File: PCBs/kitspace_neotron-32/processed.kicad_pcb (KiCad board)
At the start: 4 copper layers, 166.9 x 140.7 mm, 97 parts, among them J1001 Conn_02x05, J101 Conn_02x06, J102 Conn_02x06, J103 Conn_02x04, J201 DIN-5 180 degree, J202 DIN-5 180 degree, J301 3.5mm Audio Jack TRS, J302 Conn_01x03_Male, J401 USB_B, J501 micro SD Card, J601 Conn_02x13_Header, J701 AVR-ISP-6, J702 DE9 Male, J703 DE9 Male, J704 Double-mini-DIN-6, J901 DB15HD_Female, SW401 SW_Push_DPDT_ON_OFF, SW402 SW_Push_DPDT_ON_MO, U1001 ICL3232CPZMAX, U101 EK-TM4C123GXL, U201 74LS14, U202 6N138, U401 TC1262-33, U601 MCP23S17_SP, U701 ATmega328-PU, U801 MCP7940N-xP, Y801 32,768 Hz

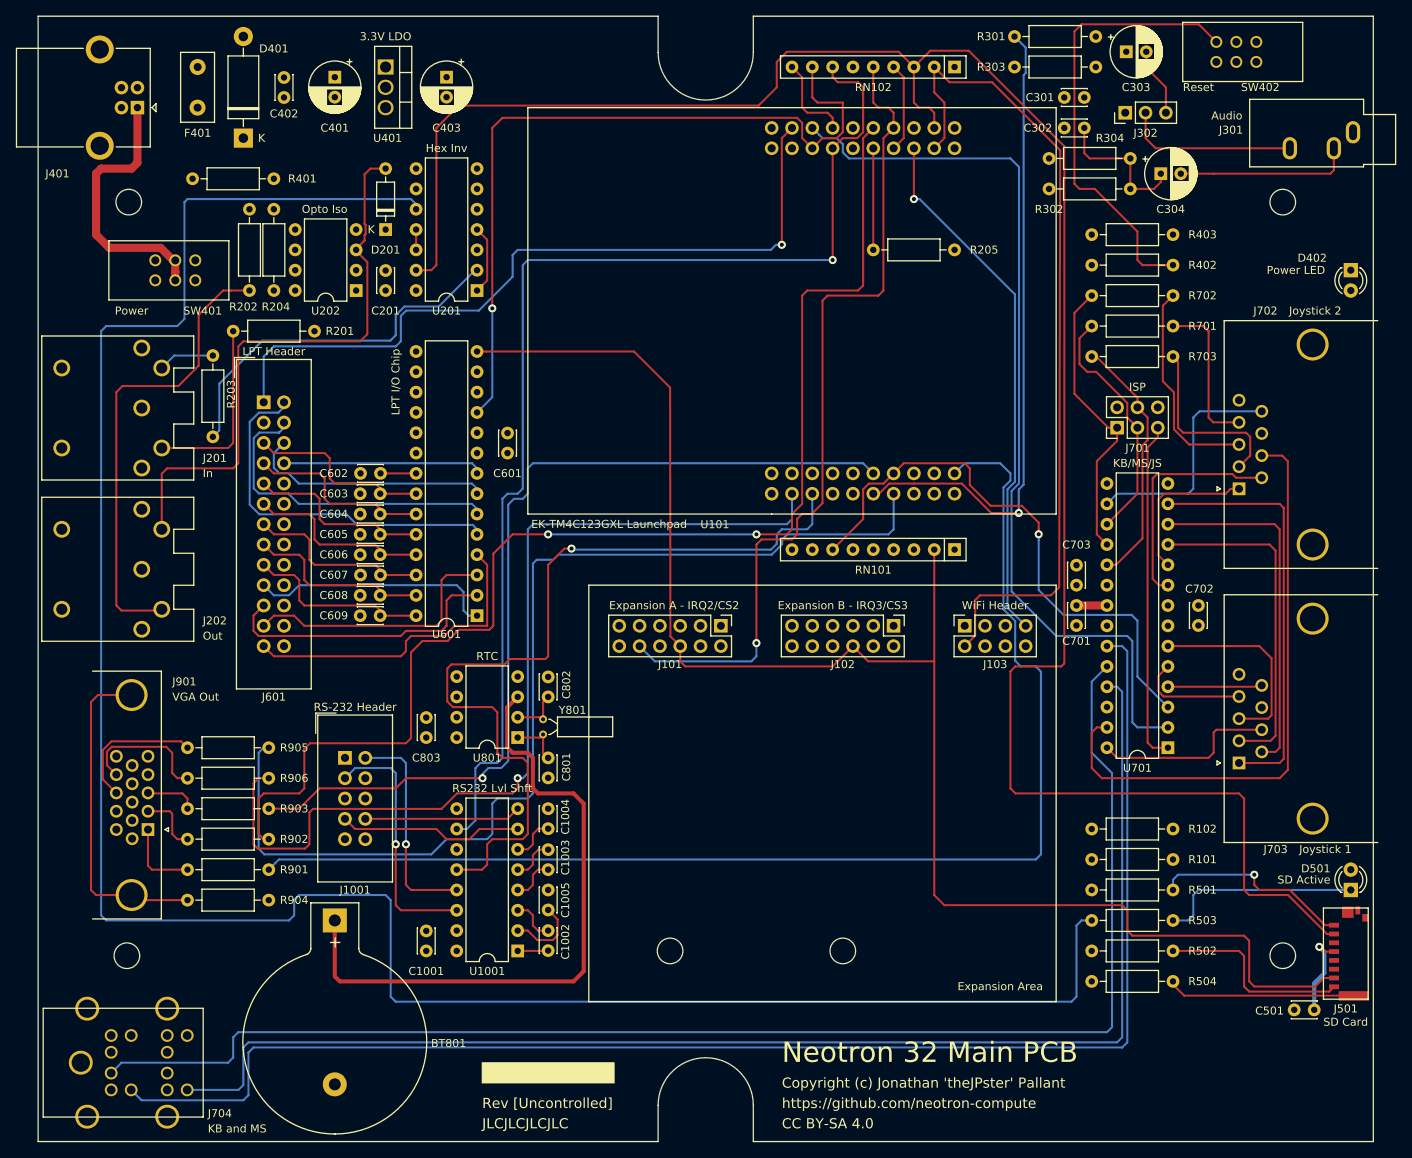
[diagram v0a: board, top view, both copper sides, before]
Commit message: recheck all circuits and clean up fill zone by rerouting the nets using freerouting and manually
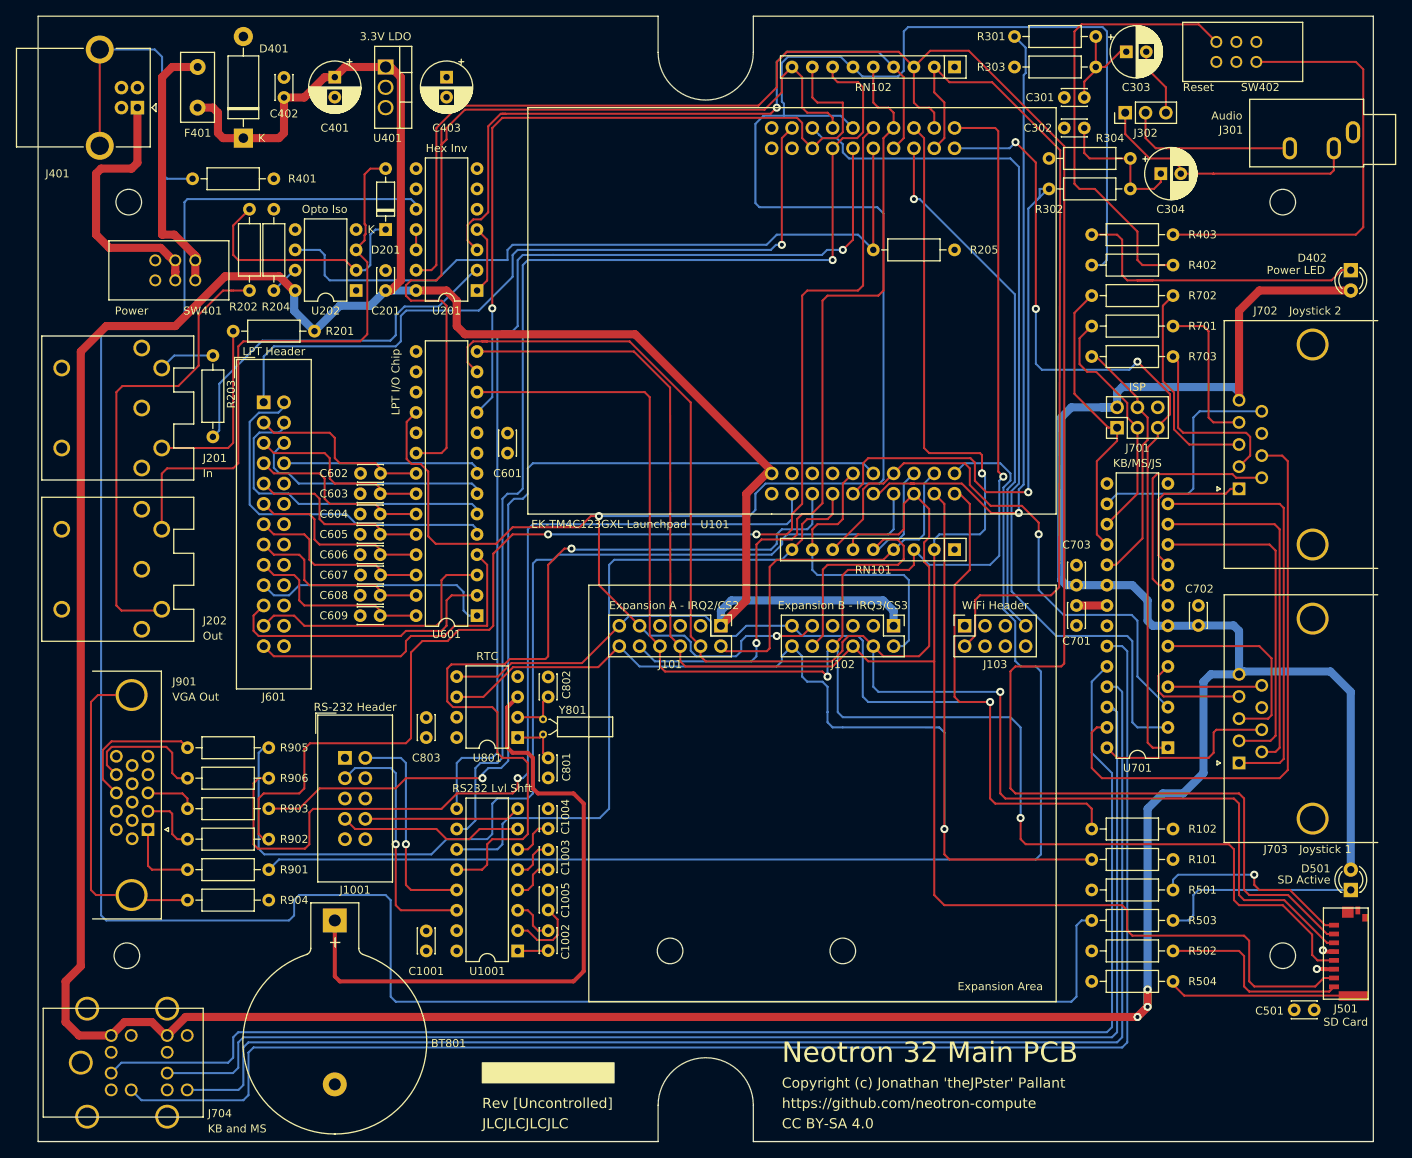
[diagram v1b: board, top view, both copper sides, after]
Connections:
- BT801 pad 2: (no net) -> GND
- C1001 pad 1: (no net) -> GND
- C1001 pad 2: (no net) -> +3V3
- C1004 pad 1: (no net) -> GND
- C1005 pad 1: (no net) -> +3V3
- C201 pad 1: (no net) -> +5V
- C201 pad 2: (no net) -> GND
- C301 pad 1: (no net) -> GND
- C301 pad 2: (no net) -> Net-(C301-Pad2)
- C302 pad 1: (no net) -> GND
- C303 pad 1: (no net) -> Net-(C301-Pad2)
- C401 pad 1: (no net) -> +5V
- C401 pad 2: (no net) -> GND
- C402 pad 1: (no net) -> +5V
- C402 pad 2: (no net) -> GND
- C403 pad 1: (no net) -> +3V3
- C403 pad 2: (no net) -> GND
- C501 pad 2: (no net) -> GND
- C601 pad 1: (no net) -> +3V3
- C601 pad 2: (no net) -> GND
- C602 pad 1: (no net) -> GND
- C603 pad 1: (no net) -> GND
- C604 pad 1: (no net) -> GND
- C605 pad 1: (no net) -> GND
- C606 pad 1: (no net) -> GND
- C607 pad 1: (no net) -> GND
- C608 pad 1: (no net) -> GND
- C609 pad 1: (no net) -> GND
- C701 pad 1: (no net) -> GND
- C702 pad 1: (no net) -> +5V
- C702 pad 2: (no net) -> GND
- C703 pad 1: (no net) -> +5V
- C703 pad 2: (no net) -> GND
- C801 pad 1: (no net) -> GND
- C802 pad 2: (no net) -> GND
- C803 pad 1: (no net) -> +3V3
- C803 pad 2: (no net) -> GND
- D201 pad 1: (no net) -> Net-(D201-Pad1)
- D401 pad 1: (no net) -> +5V
- D401 pad 2: (no net) -> GND
- D402 pad 1: (no net) -> Net-(D402-Pad1)
- D402 pad 2: (no net) -> +5V
- D501 pad 2: (no net) -> +5V
- F401 pad 1: (no net) -> +5V
- F401 pad 2: (no net) -> /Power/UNFUSED_5V
- J1001 pad 1: (no net) -> Net-(J1001-Pad1)
- J1001 pad 10: (no net) -> Net-(J1001-Pad10)
- J1001 pad 4: (no net) -> Net-(J1001-Pad4)
- J1001 pad 5: (no net) -> GND
- J1001 pad 6: (no net) -> Net-(J1001-Pad6)
- J1001 pad 9: (no net) -> Net-(J1001-Pad9)
- J101 pad 1: (no net) -> +5V
- J101 pad 11: (no net) -> /PA7_I2C_SDA
- J101 pad 12: (no net) -> /PA6_I2C_SCL
- J101 pad 2: (no net) -> /~PE3_IRQ2
- J101 pad 3: (no net) -> +3V3
- J101 pad 4: (no net) -> /PA5_SPI_MOSI
- J101 pad 5: (no net) -> GND
- J101 pad 7: (no net) -> GND
- J101 pad 8: (no net) -> /PA2_SPI_CLK
- J101 pad 9: (no net) -> /~RESET
- J102 pad 1: (no net) -> +5V
- J102 pad 10: (no net) -> /~PE2_SPI_CS3
- J102 pad 11: (no net) -> /PA7_I2C_SDA
- J102 pad 12: (no net) -> /PA6_I2C_SCL
- J102 pad 2: (no net) -> /~PD2_IRQ3
- J102 pad 3: (no net) -> +3V3
- J102 pad 4: (no net) -> /PA5_SPI_MOSI
- J102 pad 5: (no net) -> GND
- J102 pad 7: (no net) -> GND
- J102 pad 8: (no net) -> /PA2_SPI_CLK
- J102 pad 9: (no net) -> /~RESET
- J103 pad 1: (no net) -> +3V3
- J103 pad 3: (no net) -> Net-(J103-Pad3)
- J103 pad 4: (no net) -> Net-(J103-Pad4)
- J103 pad 5: (no net) -> Net-(J103-Pad5)
- J103 pad 6: (no net) -> Net-(J103-Pad6)
- J103 pad 8: (no net) -> GND
- J201 pad 1: (no net) -> Net-(J201-Pad1)
- J201 pad 2: (no net) -> GND
- J201 pad 3: (no net) -> Net-(J201-Pad3)
- J202 pad 1: (no net) -> Net-(J202-Pad1)
- J202 pad 2: (no net) -> Net-(J202-Pad2)
- J202 pad 3: (no net) -> Net-(J202-Pad3)
- J301 pad S: (no net) -> GND
- J302 pad 1: (no net) -> /Audio/LEFT_CHAN
- J401 pad 2: (no net) -> Net-(J401-Pad2)
- J401 pad 3: (no net) -> Net-(J401-Pad3)
- J401 pad 4: (no net) -> GND
- J401 pad 5: (no net) -> Net-(J401-Pad5)
- J501 pad 3: (no net) -> /PA5_SPI_MOSI
- J501 pad 5: (no net) -> /PA2_SPI_CLK
- J501 pad 6: (no net) -> GND
- J601 pad 10: (no net) -> GND
- J601 pad 12: (no net) -> GND
- J601 pad 14: (no net) -> GND
- J601 pad 16: (no net) -> GND
- J601 pad 18: (no net) -> GND
- J601 pad 20: (no net) -> GND
- J601 pad 22: (no net) -> GND
- J601 pad 24: (no net) -> GND
- J601 pad 26: (no net) -> GND
- J601 pad 3: (no net) -> /Parallel Printer/D0
- J701 pad 2: (no net) -> +5V
- J701 pad 6: (no net) -> GND
- J702 pad 5: (no net) -> +5V
- J702 pad 8: (no net) -> GND
- J703 pad 5: (no net) -> +5V
- J703 pad 8: (no net) -> GND
- J704 pad 10: (no net) -> +5V
- J704 pad 12: (no net) -> Net-(J704-Pad12)
- J704 pad 2: (no net) -> Net-(J704-Pad2)
- J704 pad 3: (no net) -> GND
- J704 pad 4: (no net) -> +5V
- J704 pad 6: (no net) -> Net-(J704-Pad6)
- J704 pad 7: (no net) -> /Keyboard, Mouse and Joystick/MS_DAT
- J704 pad 8: (no net) -> Net-(J704-Pad8)
- J704 pad 9: (no net) -> GND
- J901 pad 10: (no net) -> Net-(J901-Pad10)
- J901 pad 11: (no net) -> Net-(J901-Pad11)
- J901 pad 12: (no net) -> Net-(J901-Pad12)
- J901 pad 15: (no net) -> Net-(J901-Pad15)
- J901 pad 4: (no net) -> Net-(J901-Pad4)
- J901 pad 5: (no net) -> GND
- J901 pad 7: (no net) -> GND
- J901 pad 9: (no net) -> Net-(J901-Pad9)
- R101 pad 1: (no net) -> /PA6_I2C_SCL
- R101 pad 2: (no net) -> +3V3
- R102 pad 1: (no net) -> /PA7_I2C_SDA
- R102 pad 2: (no net) -> +3V3
- R201 pad 2: (no net) -> +5V
- R202 pad 1: (no net) -> Net-(D201-Pad1)
- R204 pad 1: (no net) -> GND
- R204 pad 2: (no net) -> Net-(R204-Pad2)
- R205 pad 2: (no net) -> +3V3
- R301 pad 1: (no net) -> Net-(C301-Pad2)
- R302 pad 2: (no net) -> /PE4_AUDIO_L
- R303 pad 1: (no net) -> Net-(C301-Pad2)
- R303 pad 2: (no net) -> GND
- R304 pad 2: (no net) -> GND
- R401 pad 1: (no net) -> GND
- R401 pad 2: (no net) -> Net-(J401-Pad5)
- R402 pad 1: (no net) -> /~RESET
- R403 pad 1: (no net) -> Net-(D402-Pad1)
- R403 pad 2: (no net) -> Net-(R403-Pad2)
- R501 pad 2: (no net) -> +3V3
- R502 pad 2: (no net) -> +3V3
- R504 pad 2: (no net) -> GND
- R904 pad 1: (no net) -> GND
- RN101 pad 1: (no net) -> GND
- RN101 pad 3: (no net) -> /PA2_SPI_CLK
- RN101 pad 4: (no net) -> /~PE3_IRQ2
- RN101 pad 5: (no net) -> /~PE2_SPI_CS3
- RN101 pad 6: (no net) -> /PA5_SPI_MOSI
- RN101 pad 8: (no net) -> /~PD2_IRQ3
- RN101 pad 9: (no net) -> /PB1_U1TX
- RN102 pad 1: (no net) -> GND
- RN102 pad 6: (no net) -> /~RESET
- SW401 pad 1: (no net) -> Net-(SW401-Pad1)
- SW401 pad 3: (no net) -> /Power/UNFUSED_5V
- SW401 pad 4: (no net) -> Net-(SW401-Pad4)
- SW401 pad 5: (no net) -> /Power/VUSB
- SW401 pad 6: (no net) -> /Power/UNFUSED_5V
- SW402 pad 1: (no net) -> Net-(SW402-Pad1)
- SW402 pad 2: (no net) -> GND
- SW402 pad 4: (no net) -> Net-(R403-Pad2)
- SW402 pad 5: (no net) -> GND
- SW402 pad 6: (no net) -> Net-(SW402-Pad6)
- U1001 pad 11: (no net) -> /PB1_U1TX
- U1001 pad 15: (no net) -> GND
- U1001 pad 16: (no net) -> +3V3
- U1001 pad 9: (no net) -> /PC5_U1CTS
- U101 pad 1.1: (no net) -> +3.3VP
- U101 pad 1.4: (no net) -> /PB1_U1TX
- U101 pad 1.5: (no net) -> /PE4_AUDIO_L
- U101 pad 1.8: (no net) -> /PA5_SPI_MOSI
- U101 pad 1.9: (no net) -> /PA6_I2C_SCL
- U101 pad 2.1: (no net) -> GND
- U101 pad 2.5: (no net) -> /~RESET
- U101 pad 2.8: (no net) -> /PA4_SPI_MISO
- U101 pad 3.2: (no net) -> GND
- U101 pad 3.3: (no net) -> Net-(U101-Pad3.3)
- U101 pad 3.4: (no net) -> Net-(U101-Pad3.4)
- U101 pad 3.5: (no net) -> /~PD2_IRQ3
- U101 pad 3.8: (no net) -> /~PE2_SPI_CS3
- U101 pad 3.9: (no net) -> /~PE3_IRQ2
- U101 pad 4.1: (no net) -> Net-(U101-Pad4.1)
- U101 pad 4.2: (no net) -> Net-(U101-Pad4.2)
- U101 pad 4.5: (no net) -> /PC5_U1CTS
- U201 pad 14: (no net) -> +5V
- U201 pad 3: (no net) -> /PC7_MIDI_OUT
- U201 pad 5: (no net) -> GND
- U201 pad 6: (no net) -> Net-(U201-Pad6)
- U201 pad 7: (no net) -> GND
- U201 pad 8: (no net) -> Net-(U201-Pad8)
- U201 pad 9: (no net) -> GND
- U202 pad 1: (no net) -> Net-(U202-Pad1)
- U202 pad 2: (no net) -> Net-(D201-Pad1)
- U202 pad 3: (no net) -> Net-(D201-Pad2)
- U202 pad 4: (no net) -> Net-(U202-Pad4)
- U202 pad 5: (no net) -> GND
- U202 pad 6: (no net) -> /PC6_MIDI_IN
- U202 pad 7: (no net) -> Net-(R204-Pad2)
- U202 pad 8: (no net) -> +5V
- U401 pad 1: (no net) -> +5V
- U401 pad 2: (no net) -> GND
- U401 pad 3: (no net) -> +3V3
- U601 pad 10: (no net) -> GND
- U601 pad 12: (no net) -> /PA2_SPI_CLK
- U601 pad 13: (no net) -> /PA5_SPI_MOSI
- U601 pad 15: (no net) -> GND
- U601 pad 16: (no net) -> GND
- U601 pad 17: (no net) -> GND
- U601 pad 18: (no net) -> /~RESET
- U601 pad 19: (no net) -> Net-(U601-Pad19)
- U601 pad 20: (no net) -> /~PF0_IRQ1
- U601 pad 9: (no net) -> +3V3
- U701 pad 14: (no net) -> Net-(U701-Pad14)
- U701 pad 15: (no net) -> Net-(U701-Pad15)
- U701 pad 20: (no net) -> +5V
- U701 pad 22: (no net) -> GND
- U701 pad 26: (no net) -> /Keyboard, Mouse and Joystick/MS_DAT
- U701 pad 7: (no net) -> +5V
- U701 pad 8: (no net) -> GND
- U801 pad 4: (no net) -> GND
- U801 pad 5: (no net) -> /PA7_I2C_SDA
- U801 pad 6: (no net) -> /PA6_I2C_SCL
- U801 pad 7: (no net) -> Net-(U801-Pad7)
- U801 pad 8: (no net) -> +3V3
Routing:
- net GND: track 4.58 -> 808.4 mm, vias 0 -> 1
- net +5V: track 0.00 -> 644.2 mm, vias 0 -> 3
- net +3V3: track 10.7 -> 357.5 mm
- net /~RESET: track 0.00 -> 279.6 mm, vias 0 -> 2
- net /PA2_SPI_CLK: track 0.00 -> 270.6 mm, vias 0 -> 3
- net /PA5_SPI_MOSI: track 0.00 -> 223.7 mm, vias 0 -> 1
- net /Keyboard, Mouse and Joystick/MS_DAT: track 0.00 -> 164.7 mm
- net /PA6_I2C_SCL: track 0.00 -> 151.0 mm, vias 0 -> 1
- net /PA7_I2C_SDA: track 0.00 -> 140.3 mm, vias 0 -> 1
- net /PC5_U1CTS: track 0.00 -> 129.2 mm, vias 0 -> 1
- net /~PF0_IRQ1: track 11.2 -> 113.1 mm
- net /PB1_U1TX: track 0.00 -> 87.3 mm
- net /PC6_MIDI_IN: track 12.7 -> 92.1 mm
- net /PC7_MIDI_OUT: track 11.2 -> 87.8 mm, vias 0 -> 1
- net /PE4_AUDIO_L: track 0.00 -> 69.6 mm, vias 0 -> 1
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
